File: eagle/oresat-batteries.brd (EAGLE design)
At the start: 94 x 93.5 mm, 82 parts, among them IC1 74AHC1G08DBV, U1 TCAN330, U2 STM32F042K6, U3 ADP5062, X1 16MHz

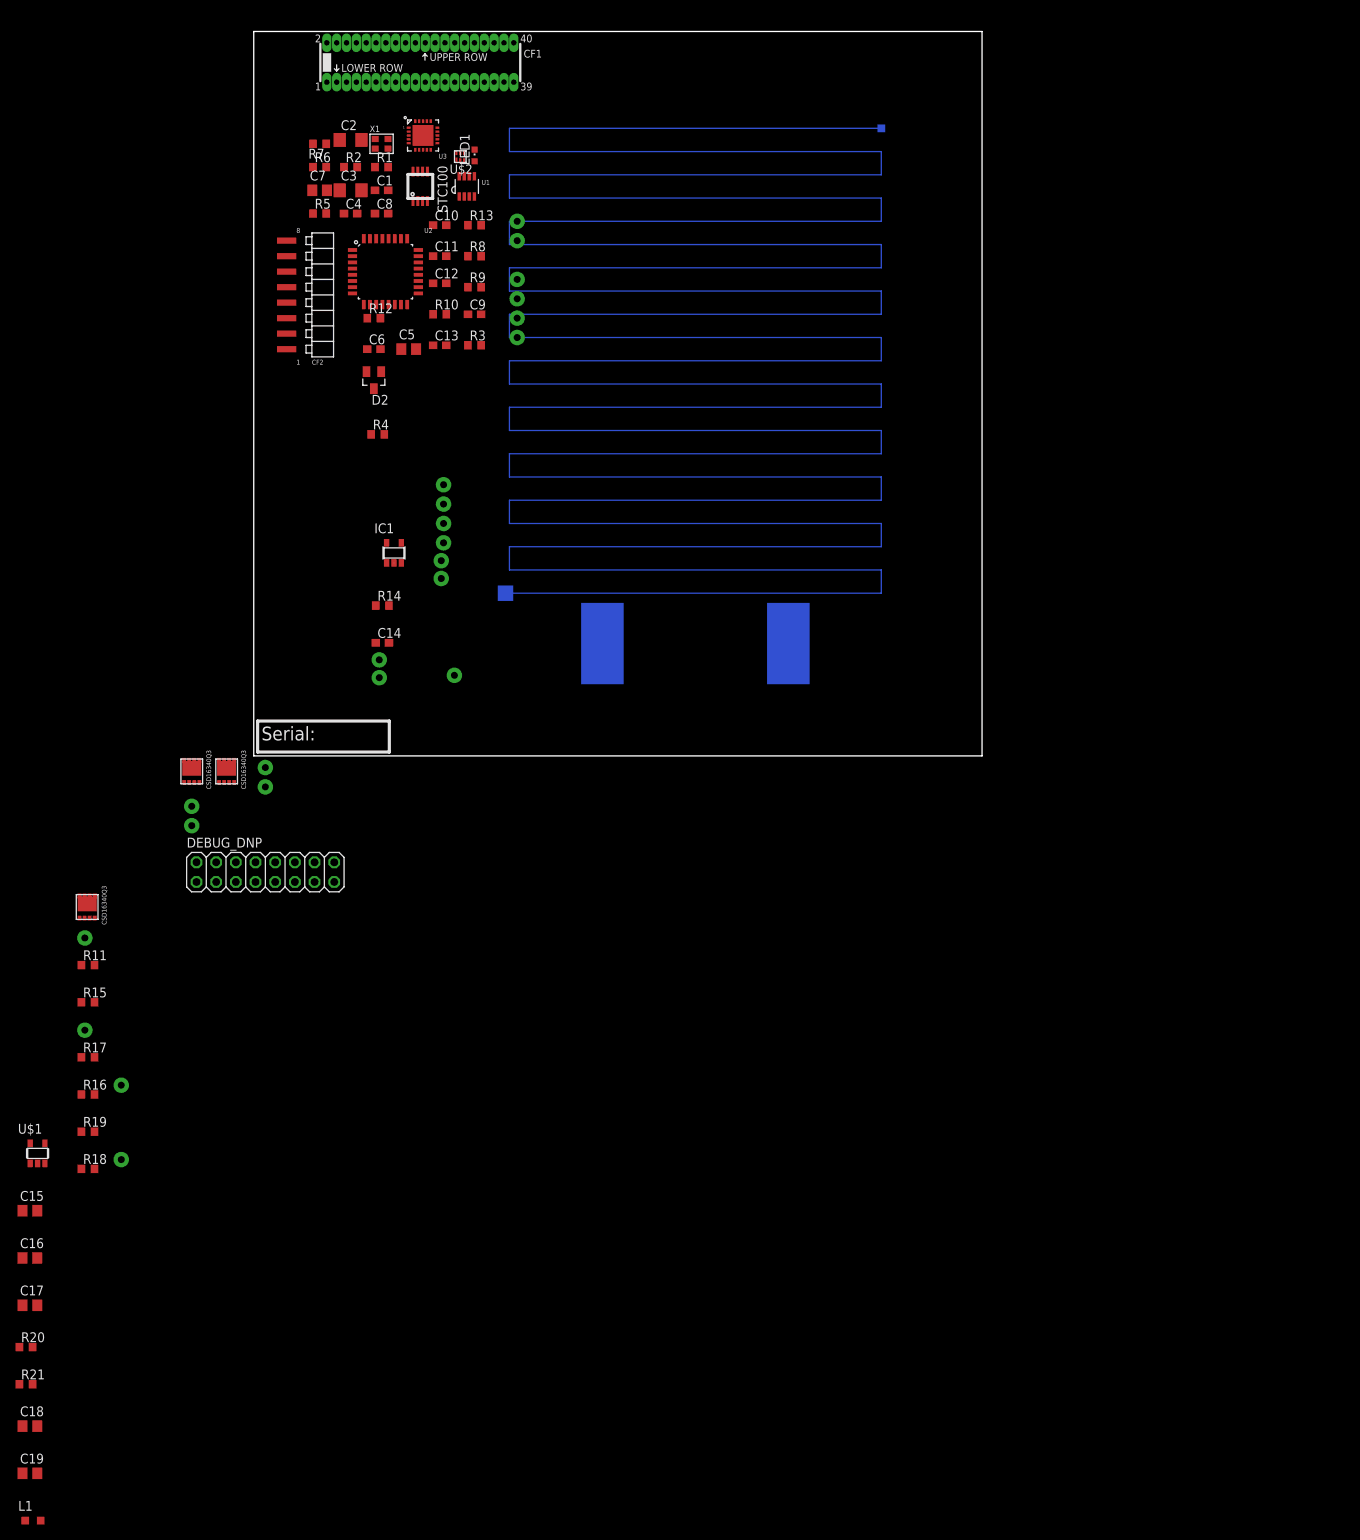
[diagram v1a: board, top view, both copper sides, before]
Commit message: First cleanup of batteries post-Austin going to NASA. Austiiiiinnnnnnnnn, come backgit diff ../design.mdn111git diff ../design.mdn./run More sane two sheet layout on schematic, cleaned up in and out arrays but it needs more thought. New OreSat card board and connector.
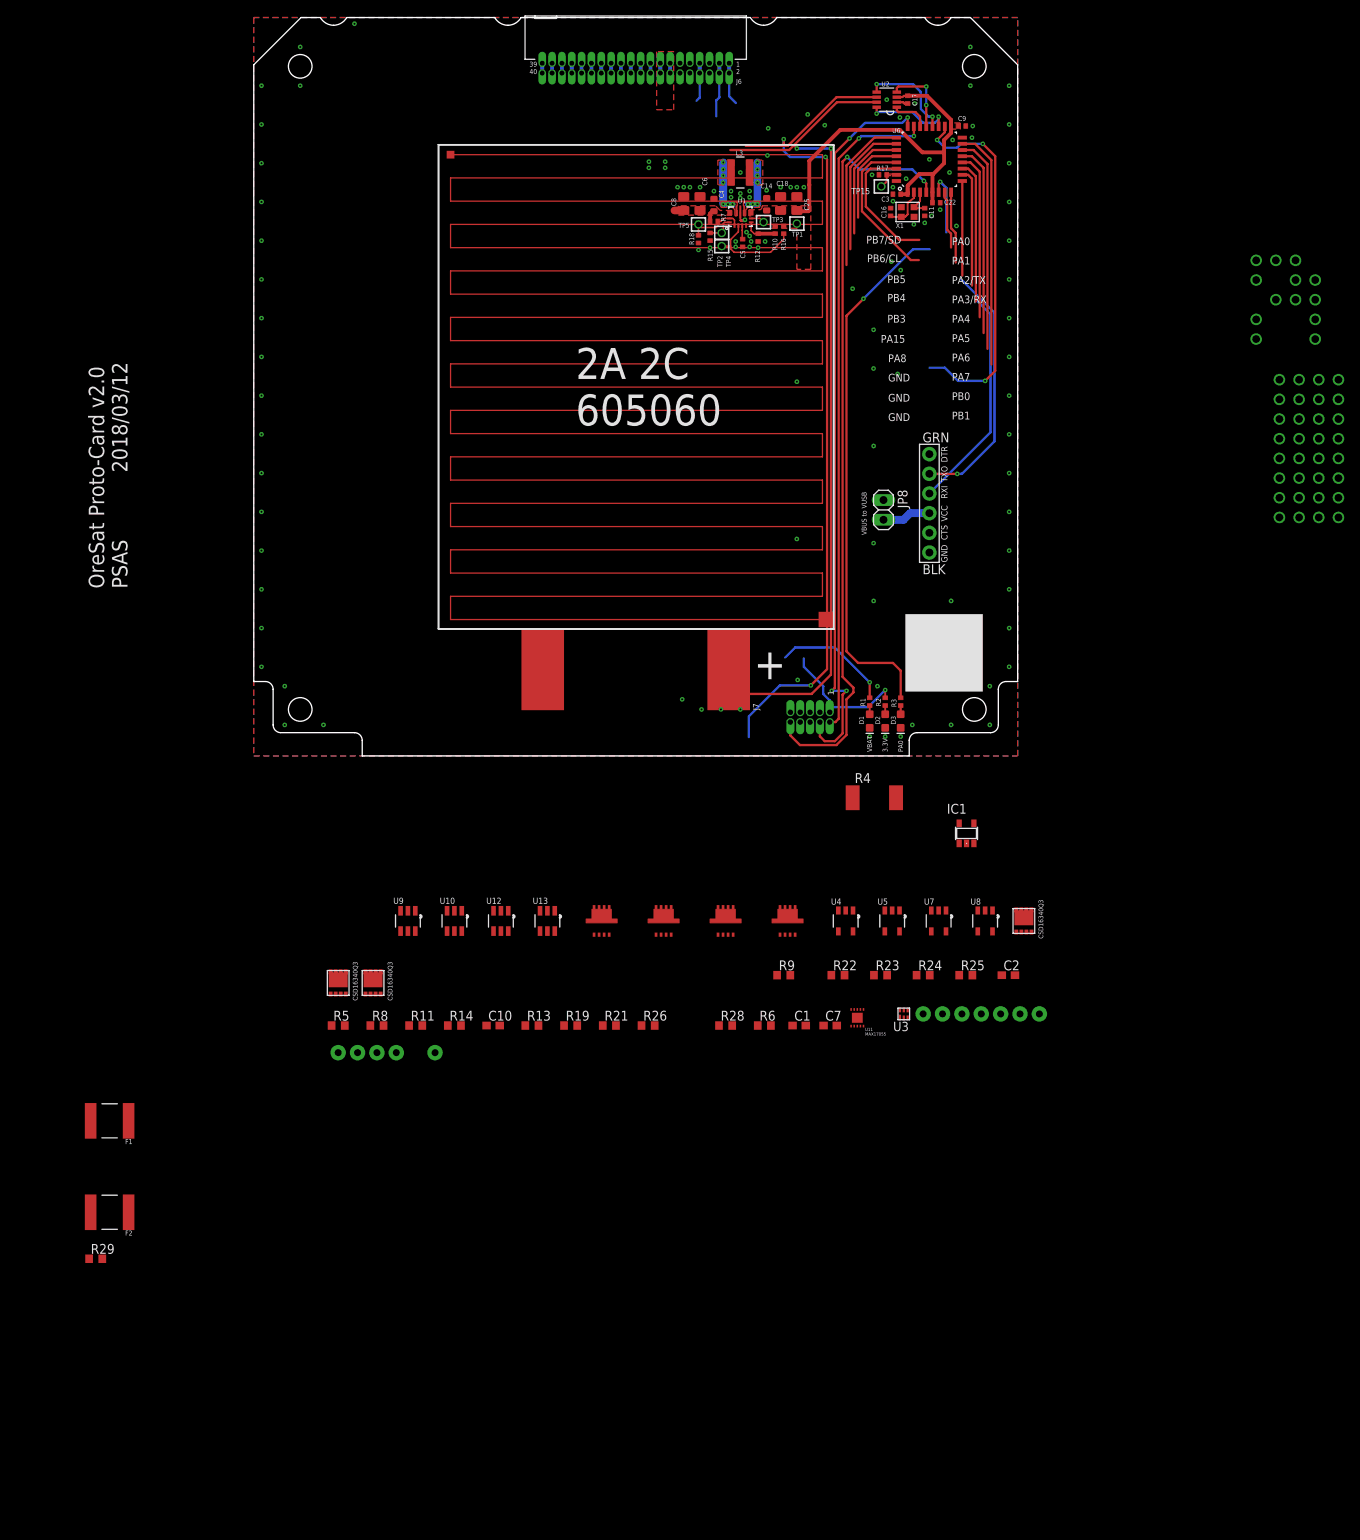
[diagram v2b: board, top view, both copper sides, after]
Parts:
- removed C12, C13: 100n, rcl:C0603
- removed C15, C19: 10u, rcl:C0805
- removed CF1: ORESAT-CONNECTOR-40PIN, low-gain-radio:HARWIN-ARCHER-M50-3202045
- removed CF2: 2MM-RA-1X8, oresat-batteries:CF-2MM-RA-1X8-PRECIDIP-831
- removed DEBUG_DNP: (no value), pinhead:2X08
- removed L1: (no value), rcl:L2012C
- removed LED1: DNP/GRN, led:CHIPLED_0603
- removed U$1: LM3761, oresat-batteries:SOT23-5
- removed U$10, U$11, U$12, U$15, U$16, U$17, U$18, U$19, U$22, U$23, U$25, U$26, U$27, U$28, U$29, U$4, U$8, U$9: TP, oresat-batteries:2MM_TP
- removed U$13, U$14, U$20: CSD16340Q3, oresat-batteries:Q3
- removed U$2: BQ2970, oresat-batteries:PSOP6
- removed U$21: 4.19, oresat-batteries:RES_HEATER
- removed U$3: 2AHBATT, oresat-batteries:2AH_605060
- removed U$5: STC3100LST, oresat-batteries:MINISO-8
- added B1: 2AHBATT, oresat-batteries:2AH_605060
- added C22: 100n, rcl_custom:.0402-B-NOSILK
- added C25: 22u, oresat-rcl:.0805-B-NOSILK
- added CARD: ORESAT-CARD-V0.5, oresat-card:ORESAT-CARD-V1.0
- added D1, D3: GREEN, SparkFun-LED:LED-0603
- added F1: 2016L200PR, F-LITTELFUSE-2016L-SERIES-PTC:2016L
- added F2: 2016L500DR, F-LITTELFUSE-2016L-SERIES-PTC:2016L
- added H1, H2, H3, H4: STAND-OFFTIGHT, SparkFun-Hardware:STAND-OFF-TIGHT
- added J5: (no value), SparkFun-Connectors:6_PIN_SERIAL_TARGET_SIDE_W_SILK
- added J6: J-SAMTEC-TFM-120-X1-XXX-D-RA, J-Samtec-TFM-120-X1-XXX-D-RA:J-SAMTEC-TFM-120-X1-XXX-D-RA
- added J7: 1.27MM-SWD-CONNECTOR, J-CNC-3220-10-0100-00-ARM-SWD-port:1.27MM_2X5
- added JP8: (no value), pinhead:1X02
- added L3: 1.5 uH, L-Coilcraft-XFL4020:L-COILCRAFT-XFL4020
- added Q1, Q2, Q7: CSD16340Q3, oresat-batteries:Q3
- added Q3, Q4, Q5, Q6: TPN4R712MD, tpn4r712md-pmosfet:TSON-ADVANCE-3X3
- added R22, R23, R24, R25: 470k, rcl:R0603
- added R26, R28, R29: 10k, rcl:R0603
- added TP10, TP11, TP12, TP13, TP14, TP16, TP17, TP20, TP6, TP7, TP8, TP9: TP, oresat-batteries:2MM_TP
- added TP15: TEST-POINT, Tova:2MM-TEST-POINT
- added U10, U12, U13, U9: LTC4412, ltc4412:SOT23-6
- added U11: MAX17055, max17055:TDFN-10L
- added U4, U5, U7, U8: LTC4411, ltc4411:SOT23-5-B
- added U6: STM32F042K6, STM32F042K:QFP32-7X7
- C10: value 100n -> .1u
- C11: value 100n -> 20p; device rcl:C0603 -> rcl_custom:.0402-B-NOSILK
- C14: value .1u -> 22u; device rcl:C0603 -> oresat-rcl:.0603-B-NOSILK
- C16: value 10u -> 20p; device rcl:C0805 -> rcl_custom:.0402-B-NOSILK
- C17, C5: value 10u -> 100n; device rcl:C0805 -> rcl_custom:.0402-B-NOSILK
- C18: value 10u -> 22u; device rcl:C0805 -> oresat-rcl:.0805-B-NOSILK
- C2: value 22u -> .47u; device rcl:C1206 -> rcl:C0603
- C3: value 22u -> 100n; device rcl:C1206 -> rcl_custom:.0402-B-NOSILK
- C4: value 10n -> 10u; device rcl:C0603 -> oresat-rcl:.0603-B-NOSILK
- C6: value .22u -> 10u; device rcl:C0603 -> oresat-rcl:.0805-B-NOSILK
- C7: value 1u -> .1u; device rcl:C0805 -> rcl:C0603
- C8: value 20p -> 10u; device rcl:C0603 -> oresat-rcl:.0805-B-NOSILK
- C9: value 20p -> 100n; device rcl:C0603 -> rcl_custom:.0402-B-NOSILK
- D2: value BAS40 -> GREEN; device diode:SOT23 -> SparkFun-LED:LED-0603
- R1: value THERMISTER -> 2.7k; device rcl:R0603 -> rcl_custom:.0402-B-NOSILK
- R10: value 10k -> 470k; device rcl:R0603 -> rcl_custom:.0402-B-NOSILK
- R11: value 10k -> 4.7k
- R12: value 10k -> 100k; device rcl:R0603 -> rcl_custom:.0402-B-NOSILK
- R13: value DNP/0 -> 10k
- R15: value DNP/10k -> 10k; device rcl:R0603 -> rcl_custom:.0402-B-NOSILK
- R16: value DNP/10K -> NP; device rcl:R0603 -> rcl_custom:.0402-B-NOSILK
- R17: device rcl:R0603 -> rcl_custom:.0402-B-NOSILK
- R18: value 10k -> NP; device rcl:R0603 -> rcl_custom:.0402-B-NOSILK
- R19: value DNP/10k -> 10k
- R2: value 220 -> 2.7k; device rcl:R0603 -> rcl_custom:.0402-B-NOSILK
- R20: value 10k -> 4.19; device rcl:R0603 -> oresat-batteries:RES_HEATER
- R3: value .01-.05 -> 2.7k; device rcl:R0603 -> rcl_custom:.0402-B-NOSILK
- R4: value 200k .1% -> .01-.05; device rcl:R0603 -> rcl:R2512
- R5: value 1k -> 2.2k
- R6: value 2.2k -> 330
- R7: value 330 -> 10k; device rcl:R0603 -> rcl_custom:.0402-B-NOSILK
- R8: value 1.6k -> 4.7k
- R9: value 1.6k -> DNP/0
- TP1, TP2, TP3, TP4, TP5: value TP -> TEST-POINT; device oresat-batteries:2MM_TP -> Tova:2MM-TEST-POINT
- U1: value TCAN330 -> TPS63070; device oresat-batteries:SOT23-8_TI-DCN -> ic-pwr-tps63070x:TPS63070X
- U2: value STM32F042K6 -> TCAN330; device oresat-batteries:QFP32-7X7 -> TCAN330:SOT23-8_TI-DCN
- U3: value ADP5062 -> BQ2970; device oresat-batteries:20_4X4_VVTQ -> oresat-batteries:PSOP6
- X1: value 16MHz -> 16MHZ-2.5x2mm
- moved C17 192.5 mm to (84.4, 84.7), turned to 90 degrees
- moved C18 185.2 mm to (68.0, 71.3), turned to 90 degrees
- moved C16 174.8 mm to (82.2, 70.2), turned to 90 degrees
- moved R17 153.3 mm to (81.2, 75.0)
- moved R20 146.8 mm to (49.4, 47.6)
- moved R18 143.6 mm to (57.4, 66.7), turned to 90 degrees
- moved R16 143.2 mm to (68.4, 67.9), turned to 90 degrees
- moved TP5 141.8 mm to (57.4, 68.6), turned to 90 degrees
- moved C2 137.2 mm to (97.4, -28.3)
- moved TP3 136.2 mm to (65.8, 68.9), turned to 90 degrees
- moved TP4 134.6 mm to (60.4, 67.5), turned to 90 degrees
- moved U3 129.2 mm to (83.9, -33.3)
- moved R15 127.3 mm to (58.9, 67.0), turned to 90 degrees
- moved C7 126.3 mm to (74.4, -34.8)
- moved R6 124.8 mm to (65.9, -34.8)
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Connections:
- removed net 3V3: C10.1, C11.1, C12.1, C13.1, DEBUG_DNP.1, DEBUG_DNP.2, R10.2, R8.2, R9.2, U$15.P$1, U$20.P$5, U$20.P$6, U$20.P$7, U$20.P$8, U$20.P$9, U1.3, U2.1, U2.17, U2.5
- removed net ADP_CBP: C4.1, U3.19
- removed net ADP_LED: LED1.C, U3.15
- removed net ADP_THR: R1.2, U3.18
- removed net BATOUT: CF1.P$3, D2.3
- removed net CANH: CF1.P$2, DEBUG_DNP.13, DEBUG_DNP.14, U$12.P$1, U1.7
- removed net CANL: CF1.P$1, DEBUG_DNP.11, DEBUG_DNP.12, U$8.P$1, U1.6
- removed net CAN_EN: U1.5, U2.20
- removed net CAN_LSTN: U1.8, U2.19
- removed net COUT: U$13.P$4, U$19.P$1, U$2.2
- removed net DIG_IO1: R11.1, R15.2, TP3.P$1, U3.5
- removed net DIG_IO2: R16.1, R17.2, TP4.P$1, U3.3
- removed net DIG_IO3: R18.1, R19.2, TP5.P$1, U3.2
- removed net IO0: R10.1, R13.2, U$5.1, U$9.P$1
- removed net ISO_S: C3.1, CF1.P$5, U3.10, U3.11, U3.9
- removed net LEDNP: LED1.A, R2.2
- removed net N$13: U$20.P$1, U$20.P$2, U$20.P$3, U$21.V+
- removed net N$2: R12.2, U2.31
- removed net N$3: C18.1, C19.1, L1.1, U$1.4
- removed net N$5: IC1.2, U$2.3, U$28.P$1
- removed net N$6: C14.1, IC1.5, R14.1
- removed net N$7: C17.1, R20.2, R21.1, U$1.3
- removed net OSC_IN: C8.1, U2.2, X1.1
- removed net OSC_OUT: C9.1, U2.3, X1.3
- removed net ROSC: R4.2, U$5.2
- removed net STC_CG: U$14.P$1, U$14.P$2, U$14.P$3, U$2.4, U$3.NEG
- removed net STC_IO: R13.1, U2.28
- removed net STC_VIN: C6.2, R5.1, U$5.8
- removed net STM_DEBUG: CF2.8, U2.6
- removed net SYS_EN: TP2.P$1, U2.14, U3.16
- removed net USART2_RX: CF2.7, DEBUG_DNP.5, DEBUG_DNP.6, U2.9
- removed net USART2_TX: CF2.6, DEBUG_DNP.3, DEBUG_DNP.4, U2.8
- removed net VBATT+: C2.1, C7.2, CF2.2, D2.1, R5.2, R7.2, U$29.P$1, U$3.POS, U$5.7, U3.12, U3.13, U3.14, U3.4
- removed net VSOLAR: C15.1, C16.1, C5.1, CF1.P$4, DEBUG_DNP.7, DEBUG_DNP.8, R11.2, R16.2, R18.2, R21.2, TP1.P$1, U$1.1, U3.6, U3.7, U3.8
- new net !SHUTDOWN: J6.7, J6.8
- new net 3.3V: C14.1, C17.2, C18.1, C22.2, C25.1, C3.2, C9.2, J7.VTREF, R10.2, R11.2, R13.2, R16.2, R2.2, R22.1, R23.1, R24.1, R25.1, R8.2, TP1.1, U1.7-8, U2.3, U6.1, U6.17, U6.5
- new net 4411MB: U7.5, U8.1
- new net 4411_MT: U4.5, U5.1
- new net ALERT: R13.1, R9.2, TP17.P$1, U11.8
- new net BATT-: B1.NEG, IC1.3, Q1.P$1, Q1.P$2, Q1.P$3, TP20.P$1, U3.4
- new net BGDOUT: IC1.2, TP10.P$1, U3.3
- new net BOOT: R17.2, TP15.1, U6.31
- new net BQCOUT: Q2.P$4, TP9.P$1, U3.2
- new net CAN_H: J6.3, J6.4, U2.7
- new net CAN_L: J6.1, J6.2, U2.6
- new net CAN_SHDN: U2.5, U6.20
- new net CAN_SILENT: U2.8, U6.19
- new net CHARGE-STAT-U4-U5: R25.2, U4.4, U5.4
- new net CHARGE-STAT-U7-U8: R24.2, U7.4, U8.4
- new net CHARGE_ENABLE: R29.2, TP11.P$1, U4.3, U5.3, U7.3, U8.3
- new net CRYSTALIN: C16.1, U6.2, X1.1
- new net CRYSTALOUT: C11.1, U6.3, X1.3
- new net DISCHARGE-STAT-U10-U13: R23.2, U12.4, U9.4
- new net DISCHARGE-STAT-U9-U12: R22.2, U10.4, U13.4
- new net DISCHARGE_ENABLE: R26.1, TP14.P$1, U10.3, U12.3, U13.3, U9.3
- new net INFUSE: F1.1, U4.1, U7.1
- new net MAX_IO: R9.1
- new net N$270: D1.A, R1.1
- new net N$271: D2.A, R2.1
- new net N$406: J5.P$4, JP8.2
- new net N$435: Q7.P$1, Q7.P$2, Q7.P$3, R20.V+
- new net N$436: Q5.4, U12.5
- new net N$437: Q3.1, Q3.2, Q3.3, Q5.5, Q5.6, Q5.7, Q5.8, U12.1, U9.6
- new net N$438: Q3.4, U9.5
- new net N$439: Q6.4, U13.5
- new net N$440: Q4.1, Q4.2, Q4.3, Q6.5, Q6.6, Q6.7, Q6.8, U10.6, U13.1
- new net N$441: Q4.4, U10.5
- new net OUTFUSE: F2.2, Q5.1, Q5.2, Q5.3, Q6.1, Q6.2, Q6.3, U12.6, U13.6
- new net PA0: R3.2, U6.6
- new net PA1: U6.7
- new net PA15: U6.25
- new net PA2/USART2_TX: J5.P$2, U6.8
- new net PA3/USART2_RX: J5.P$3, U6.9
- new net PA4: U6.10
- new net PA5/SPI1_SCK: U6.11
- new net PA6/SPI1_MISO: U6.12
- new net PA7/SPI1_MOSI: U6.13
- new net PB0: U6.14
- new net PB1: U6.15
- new net PB3: U6.26
- new net PB4: U6.27
- new net PB5: U6.28
- new net PB6/SCL: U6.29
- new net PB7/SDA: U6.30
- new net REG: C2.1, U11.7
- new net SPARE1: J6.17, J6.18
- new net SPARE10: J6.35, J6.36
- new net SPARE11: J6.37, J6.38
- new net SPARE12: J6.39, J6.40
- new net SPARE2: J6.19, J6.20
- new net SPARE3: J6.21, J6.22
- new net SPARE4: J6.23, J6.24
- new net SPARE5: J6.25, J6.26
- new net SPARE6: J6.27, J6.28
- new net SPARE7: J6.29, J6.30
- new net SPARE8: J6.31, J6.32
- new net SPARE9: J6.33, J6.34
- new net SYSSHD: IC1.1, R14.2, TP8.P$1
- new net TEMPSENSE: R19.1, R21.2, U11.2
- new net THRM: R19.2, U11.9
- new net TPS-EN1: R18.2, R7.1, TP5.1, U1.1, U1.14
- new net TPS-FB1: R10.1, R12.2, U1.5
- new net TPS-FB3: TP3.1, U1.6
- new net TPS-L3: L3.1, U1.11
- new net TPS-L4: L3.2, U1.9
- new net TPS-PG1: R16.1, TP2.1, U1.2
- new net TPS-VAUX1: C5.1, U1.3
- new net TPS-VSEL1: R15.2, TP4.1, U1.15
- new net VBUS: C4.1, C6.1, C8.1, F1.2, F2.1, J6.13, J6.14, J6.15, J6.16, JP8.1, R1.2, R7.2, U1.12-13
- new net V_BATT: B1.POS, C10.1, C7.1, IC1.5, Q3.5, Q3.6, Q3.7, Q3.8, Q4.5, Q4.6, Q4.7, Q4.8, Q7.P$5, Q7.P$6, Q7.P$7, Q7.P$8, Q7.P$9, R14.1, R28.2, R6.2, TP12.P$1, U10.1, U11.10, U5.5, U8.5, U9.1
- net ANDDRIVE: now also Q1.P$4; no longer U$14.P$4
- net BETSHUT: now also Q1.P$5, Q1.P$6, Q1.P$7, Q1.P$8, Q1.P$9, Q2.P$5, Q2.P$6, Q2.P$7, Q2.P$8, Q2.P$9; no longer U$13.P$5, U$13.P$6, U$13.P$7, U$13.P$8, U$13.P$9, U$14.P$5, U$14.P$6, U$14.P$7, U$14.P$8, U$14.P$9
- net BQBAT: now also R6.1, TP6.P$1, U3.5; no longer CF1.P$6, IC1.1, R14.2, R7.1, U$2.5, U$26.P$1, U$4.P$1
- net BQVMIN: now also R5.1, U3.6; no longer R6.1, U$2.6
- net CAN_RX: now also U2.4, U6.21; no longer U1.4, U2.21
- net CAN_TX: now also U2.1, U6.22; no longer U1.1, U2.22
- net C_SENSE: now also Q2.P$1, Q2.P$2, Q2.P$3, R21.1, R4.2, R5.2, TP13.P$1, U11.6; no longer R3.2, U$13.P$1, U$13.P$2, U$13.P$3, U$18.P$1, U$5.6
- net GND: now also C17.1, C22.1, C25.2, C3.1, C6.2, C7.2, C9.1, D1.C, D2.C, D3.C, J5.P$6, J6.10, J6.11, J6.12, J6.5, J6.6, J6.9, J7.GND, J7.GND@2, J7.GNDDET, R18.1, R20.V-, R26.2, R29.1, U1.10, U1.4, U10.2, U11.5, U12.2, U13.2, U2.2, U4.2, U5.2, U6.16, U6.32, U7.2, U8.2, U9.2; no longer C12.2, C13.2, C15.2, C17.2, C19.2, C3.2, C6.1, C7.1, C9.2, CF2.1, DEBUG_DNP.15, DEBUG_DNP.16, IC1.3, R1.1, R19.1, R2.1, R20.1, R3.1, R6.2, U$1.2, U$16.P$1, U$17.P$1, U$21.V-, U$22.P$1, U$23.P$1, U$5.5, U1.2, U2.16, U2.32, U3.20, U3.P$1
- net HEAT: now also Q7.P$4, R28.1; no longer U$20.P$4, U2.7
- net N$1: now also D3.A, R3.1; no longer L1.2, U$1.5
- net NRESET: now also J7.!RESET, U6.4; no longer CF2.3, U$25.P$1, U2.4
- net PA8: now also U6.18; no longer U$27.P$1, U2.18
- net SCL: now also R11.1, TP7.P$1, U11.3; no longer R9.1, U$10.P$1, U$5.4, U2.29, U3.1
- net SDA: now also TP16.P$1, U11.4; no longer U$11.P$1, U$5.3, U2.30, U3.17
- net SWCLK: now also J7.SWDCLK, U6.24; no longer CF2.4, U2.24
- net SWDIO: now also J7.SWDIO, U6.23; no longer CF2.5, U2.23
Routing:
- net CAN_H: track 0.00 -> 116.3 mm, vias 0 -> 2
- net CAN_L: track 0.00 -> 114.5 mm, vias 0 -> 3
- net NRESET: track 0.00 -> 98.8 mm, vias 0 -> 2
- net SWCLK: track 0.00 -> 95.1 mm, vias 0 -> 4
- net SWDIO: track 0.00 -> 85.8 mm, vias 0 -> 2
- net PA0: track 0.00 -> 77.4 mm, vias 0 -> 2
- net 3.3V: track 0.00 -> 71.7 mm, vias 0 -> 1
- net PA8: track 0.00 -> 48.4 mm, vias 0 -> 3
- net PA2/USART2_TX: track 0.00 -> 42.2 mm, vias 0 -> 1
- net PA3/USART2_RX: track 0.00 -> 41.5 mm
- net PB1: track 0.00 -> 31.0 mm
- net PB0: track 0.00 -> 27.9 mm
- net PA7/SPI1_MOSI: track 0.00 -> 24.7 mm
- net PA6/SPI1_MISO: track 0.00 -> 21.5 mm
- net VBUS: track 0.00 -> 21.2 mm, vias 0 -> 1
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- added copper zone on layer 1, net 3.3V
- added copper zone on layer 1, net BOOT
- added copper zone on layer 1, net GND
- added copper zone on layer 16, net GND
- added copper zone on layer 1, net TPS-L3
- added copper zone on layer 1, net TPS-L4
- added copper zone on layer 1, net VBUS
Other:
- board size 94 x 93.5 mm -> 98.6 x 95.3 mm
- board text added: "2018/03/12"
- board text added: "3.3V"
- board text added: "GND"
- board text added: "OreSat Proto-Card v2.0"
- board text added: "PA0"
- board text added: "PA1"
- board text added: "PA15"
- board text added: "PA2/TX"
- board text added: "PA3/RX"
- board text added: "PA4"
- board text added: "PA5"
- board text added: "PA6"
- board text added: "PA7"
- board text added: "PA8"
- board text added: "PB0"
- board text added: "PB1"
- board text added: "PB3"
- board text added: "PB4"
- board text added: "PB5"
- board text added: "PB6/CL"
- board text added: "PB7/SD"
- board text added: "PSAS"
- board text added: "VBAT"
- board text added: "VBUS to VUSB"
- board text removed: "Serial:"

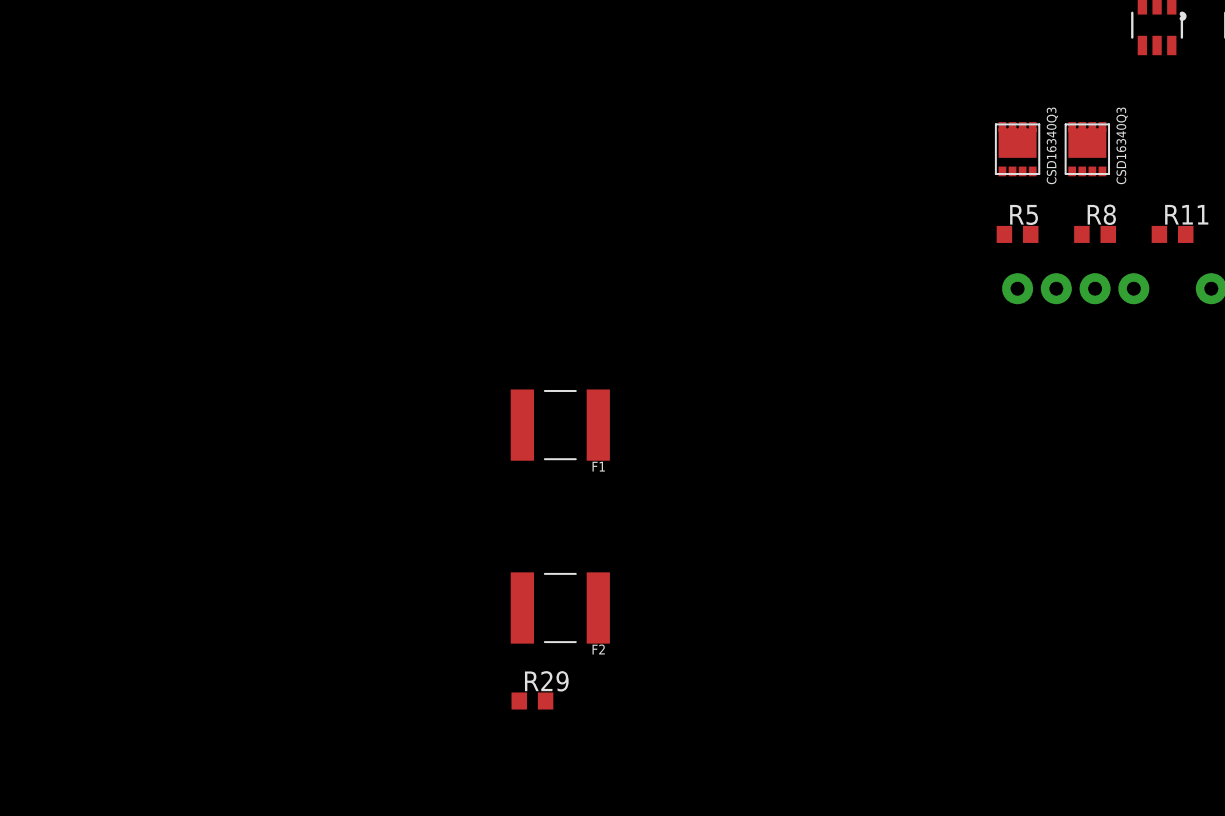
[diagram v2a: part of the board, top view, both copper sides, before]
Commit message: Fixed body diode issue on output.  Changed N to P mosfett for 'trace heater.'
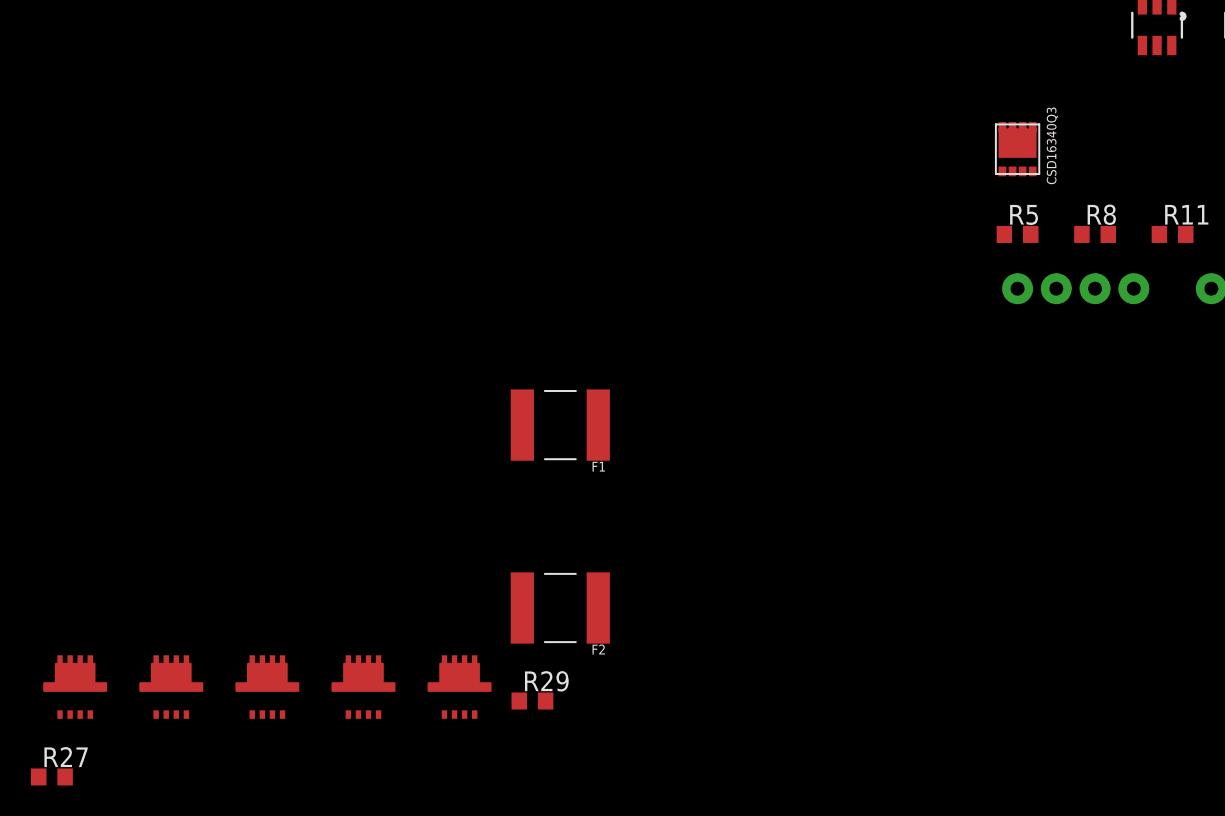
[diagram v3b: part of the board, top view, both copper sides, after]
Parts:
- removed Q7: CSD16340Q3, oresat-batteries:Q3
- added Q10, Q11, Q12, Q8, Q9: TPN4R712MD, tpn4r712md-pmosfet:TSON-ADVANCE-3X3
- added R27: 100k, rcl:R0603
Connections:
- removed net N$440: Q4.1, Q4.2, Q4.3, Q6.5, Q6.6, Q6.7, Q6.8, U10.6, U13.1
- new net .3556: Q4.5, Q4.6, Q4.7, Q4.8, Q9.5, Q9.6, Q9.7, Q9.8, U10.6, U13.1
- new net N$2: Q3.1, Q3.2, Q3.3, Q8.1, Q8.2, Q8.3
- new net N$3: Q10.1, Q10.2, Q10.3, Q5.1, Q5.2, Q5.3
- new net N$4: Q11.1, Q11.2, Q11.3, Q4.1, Q4.2, Q4.3
- new net N$5: Q6.1, Q6.2, Q6.3, Q9.1, Q9.2, Q9.3
- net GND: now also R27.1
- net HEAT: now also Q12.4, R27.2; no longer Q7.P$4
- net N$435: now also Q12.1, Q12.2, Q12.3; no longer Q7.P$1, Q7.P$2, Q7.P$3
- net N$436: now also Q10.4
- net N$437: now also Q10.5, Q10.6, Q10.7, Q10.8, Q3.5, Q3.6, Q3.7, Q3.8; no longer Q3.1, Q3.2, Q3.3, Q5.5, Q5.6, Q5.7, Q5.8
- net N$438: now also Q8.4
- net N$439: now also Q9.4
- net N$441: now also Q11.4
- net OUTFUSE: now also Q5.5, Q5.6, Q5.7, Q5.8, Q6.5, Q6.6, Q6.7, Q6.8; no longer Q5.1, Q5.2, Q5.3, Q6.1, Q6.2, Q6.3
- net V_BATT: now also Q11.5, Q11.6, Q11.7, Q11.8, Q12.5, Q12.6, Q12.7, Q12.8, Q8.5, Q8.6, Q8.7, Q8.8; no longer Q3.5, Q3.6, Q3.7, Q3.8, Q4.5, Q4.6, Q4.7, Q4.8, Q7.P$5, Q7.P$6, Q7.P$7, Q7.P$8, Q7.P$9
